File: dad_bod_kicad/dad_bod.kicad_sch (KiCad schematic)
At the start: 67 parts

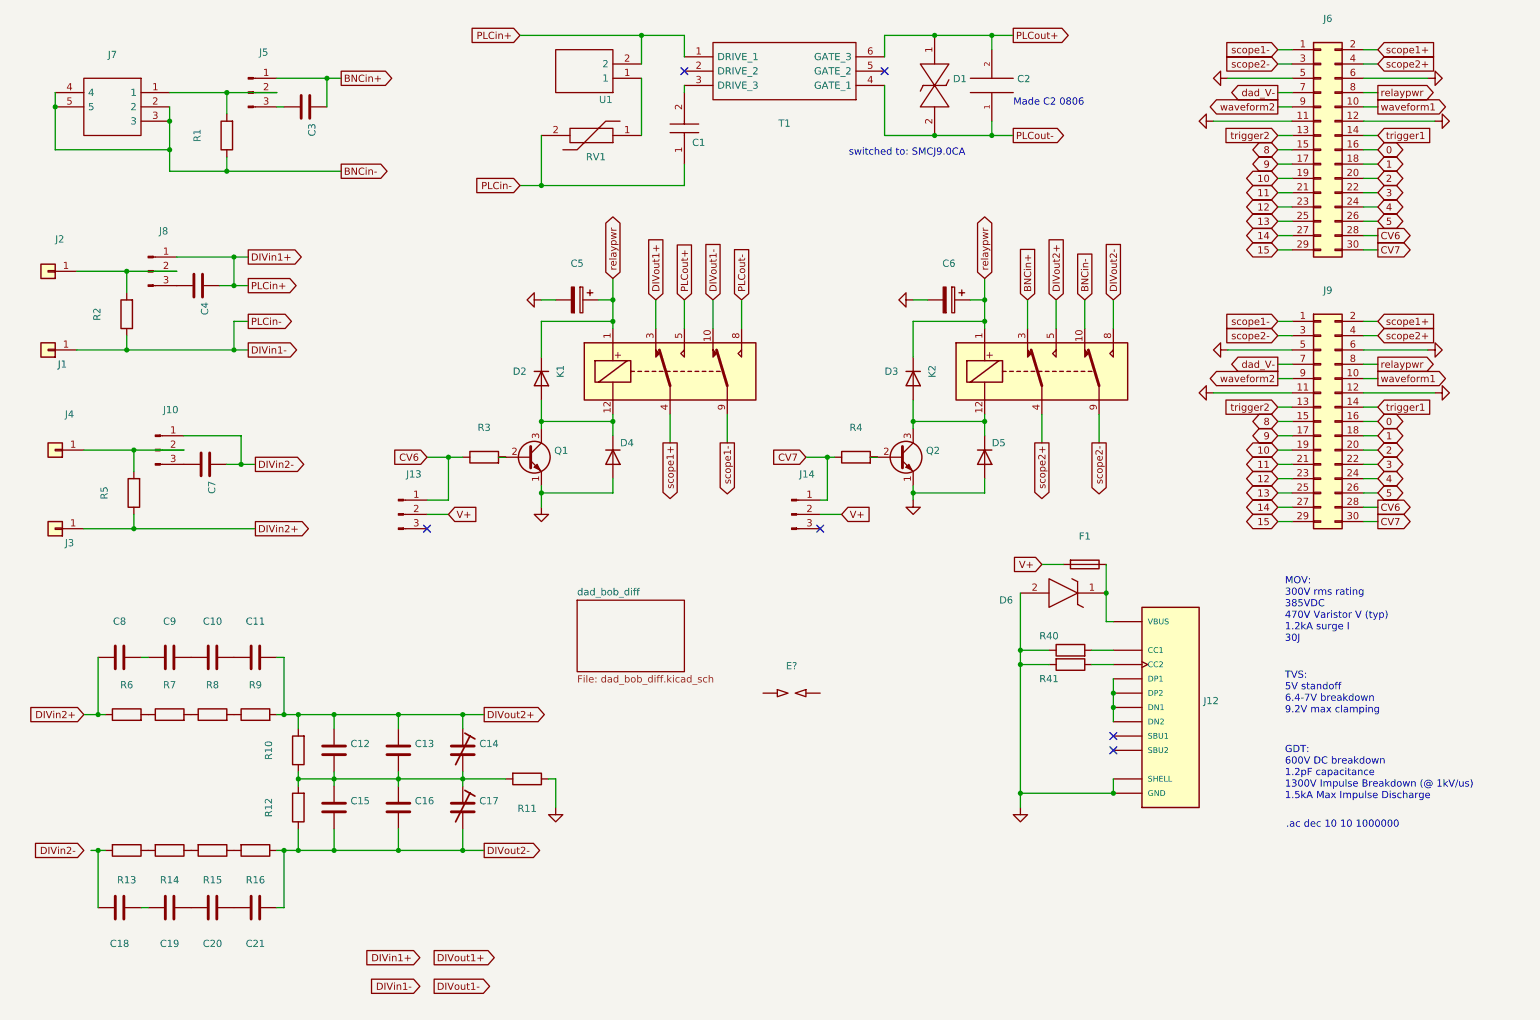
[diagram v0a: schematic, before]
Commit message: Routed PCB, layout needs rework, forked to dad_bod
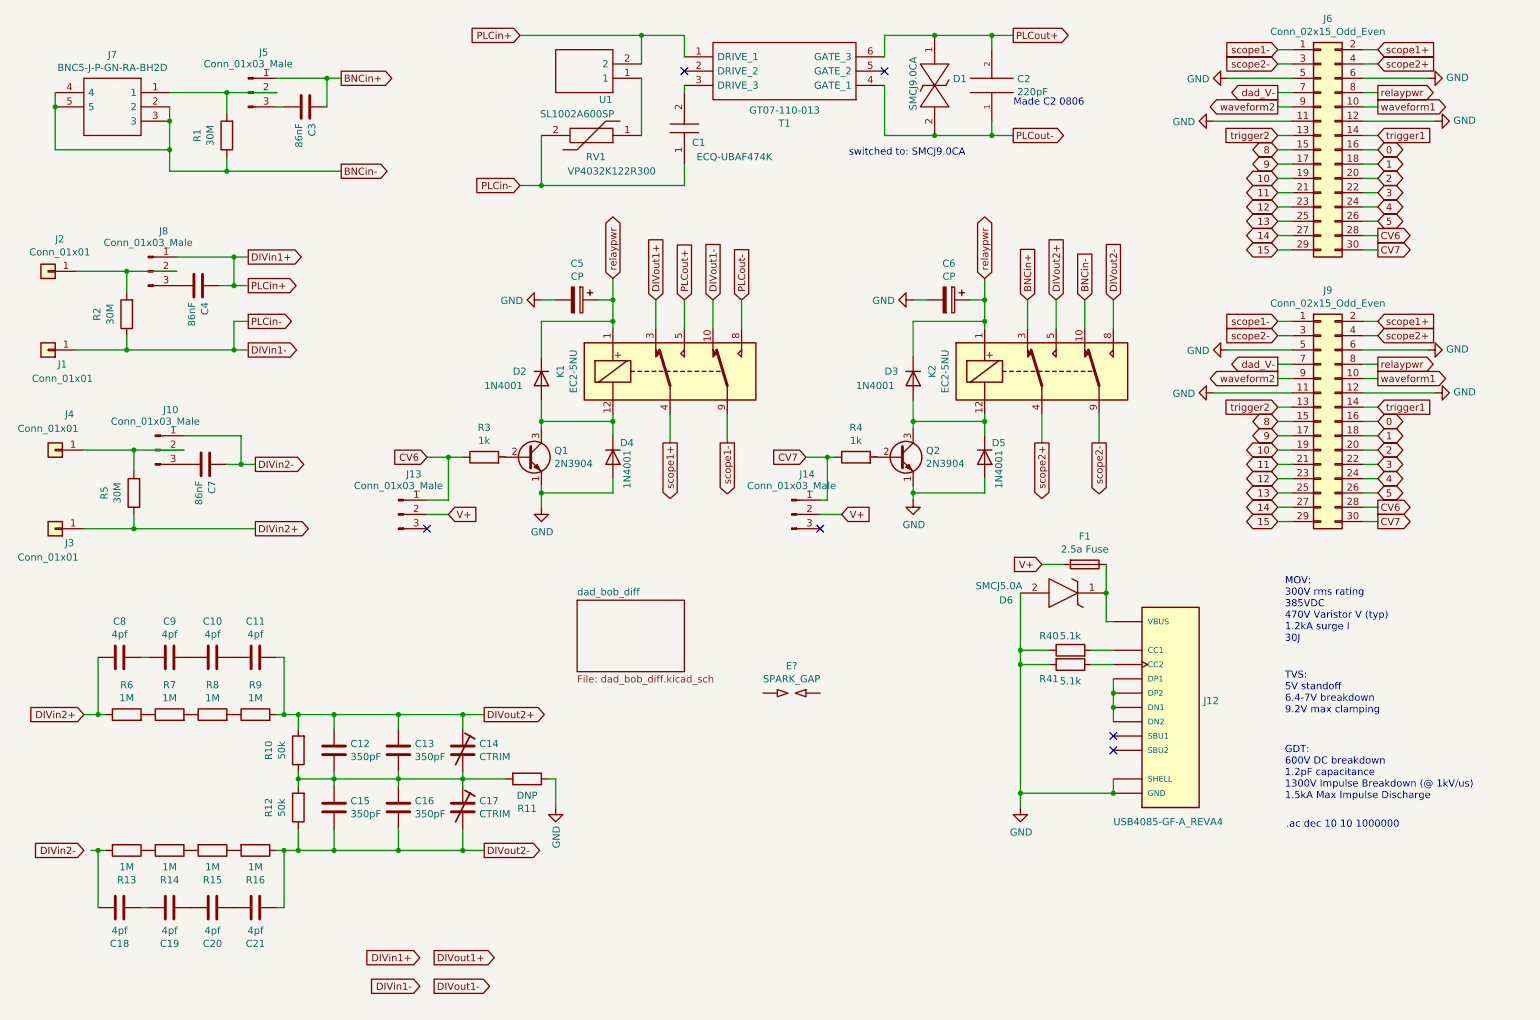
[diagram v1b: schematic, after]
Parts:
- C1: value (none) -> ECQ-UBAF474K; footprint (none) -> ECQUBAF474K
- C10, C11, C18, C19, C20, C21, C8, C9: value (none) -> 4pf; footprint (none) -> Capacitor_SMD:C_0805_2012Metric_Pad1.15x1.40mm_HandSolder
- C12, C13, C15, C16: value (none) -> 350pF; footprint (none) -> Capacitor_SMD:C_0805_2012Metric_Pad1.15x1.40mm_HandSolder
- C14, C17: value (none) -> CTRIM; footprint (none) -> Capacitor_SMD:C_Trimmer_Voltronics_JQ
- C2: value (none) -> 220pF; footprint (none) -> Capacitor_SMD:C_0805_2012Metric_Pad1.15x1.40mm_HandSolder
- C3, C4, C7: value (none) -> 86nF; footprint (none) -> Capacitor_SMD:C_0805_2012Metric_Pad1.15x1.40mm_HandSolder
- C5, C6: value (none) -> CP; footprint (none) -> Capacitor_SMD:C_0805_2012Metric_Pad1.15x1.40mm_HandSolder
- D1: value (none) -> SMCJ9.0CA; footprint (none) -> SMCJ5:DIONM7959X262N
- D2, D3, D4, D5: value (none) -> 1N4001; footprint (none) -> Diode_THT:D_DO-41_SOD81_P10.16mm_Horizontal
- D6: value (none) -> SMCJ5.0A; footprint (none) -> kyuditsky_kicad_fp:littlefuseTVS
- E?: value (none) -> SPARK_GAP
- F1: value (none) -> 2.5a Fuse; footprint (none) -> Resistor_THT:R_Axial_DIN0204_L3.6mm_D1.6mm_P2.54mm_Vertical
- J1, J2, J3, J4: value (none) -> Conn_01x01; footprint (none) -> kyuditsky_kicad_fp:Banana_Jack_S_RA_73099
- J10, J13, J14, J5, J8: value (none) -> Conn_01x03_Male; footprint (none) -> Connector_PinHeader_2.54mm:PinHeader_1x03_P2.54mm_Vertical
- J12: value (none) -> USB4085-GF-A_REVA4; footprint (none) -> GCT_USB4085-GF-A_REVA4
- J6: value (none) -> Conn_02x15_Odd_Even; footprint (none) -> Connector_PinHeader_2.54mm:PinHeader_2x15_P2.54mm_Horizontal
- J7: value (none) -> BNC5-J-P-GN-RA-BH2D; footprint (none) -> BNC5-J-P-GN-RA-BH2D_kicad:BNC5JPGNRABH2D
- J9: value (none) -> Conn_02x15_Odd_Even; footprint (none) -> Connector_PinSocket_2.54mm:PinSocket_2x15_P2.54mm_Horizontal
- K1, K2: value (none) -> EC2-5NU; footprint (none) -> Relay_THT:Relay_DPDT_Kemet_EC2
- Q1, Q2: value (none) -> 2N3904; footprint (none) -> Package_TO_SOT_THT:TO-92_Inline
- R1, R2, R5: value (none) -> 30M; footprint (none) -> Resistor_SMD:R_0805_2012Metric_Pad1.15x1.40mm_HandSolder
- R10, R12: value (none) -> 50k; footprint (none) -> Resistor_SMD:R_0805_2012Metric_Pad1.15x1.40mm_HandSolder
- R11: value (none) -> DNP; footprint (none) -> Resistor_SMD:R_0805_2012Metric_Pad1.15x1.40mm_HandSolder
- R13, R14, R15, R16, R6, R7, R8, R9: value (none) -> 1M; footprint (none) -> Resistor_SMD:R_0805_2012Metric_Pad1.15x1.40mm_HandSolder
- R3, R4: value (none) -> 1k; footprint (none) -> Resistor_SMD:R_0805_2012Metric_Pad1.15x1.40mm_HandSolder
- R40, R41: value (none) -> 5.1k; footprint (none) -> Resistor_SMD:R_0805_2012Metric_Pad1.15x1.40mm_HandSolder
- RV1: value (none) -> VP4032K122R300; footprint (none) -> VP4032K122R300_kicad:CAPPM10080X500N
- T1: value (none) -> GT07-110-013; footprint (none) -> kyuditsky_kicad_fp:GT07110013
- U1: value (none) -> SL1002A600SP; footprint (none) -> SL1002A600SP

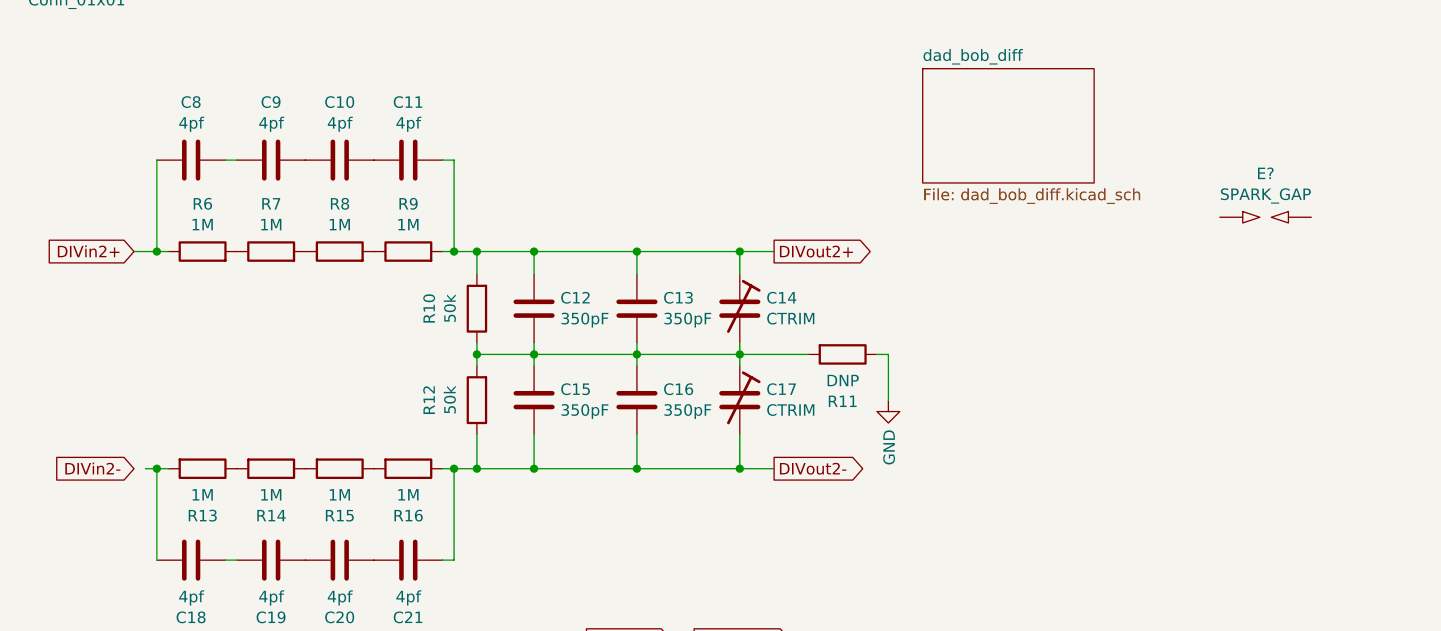
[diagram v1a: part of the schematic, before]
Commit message: fixing scheme & pcb disparities
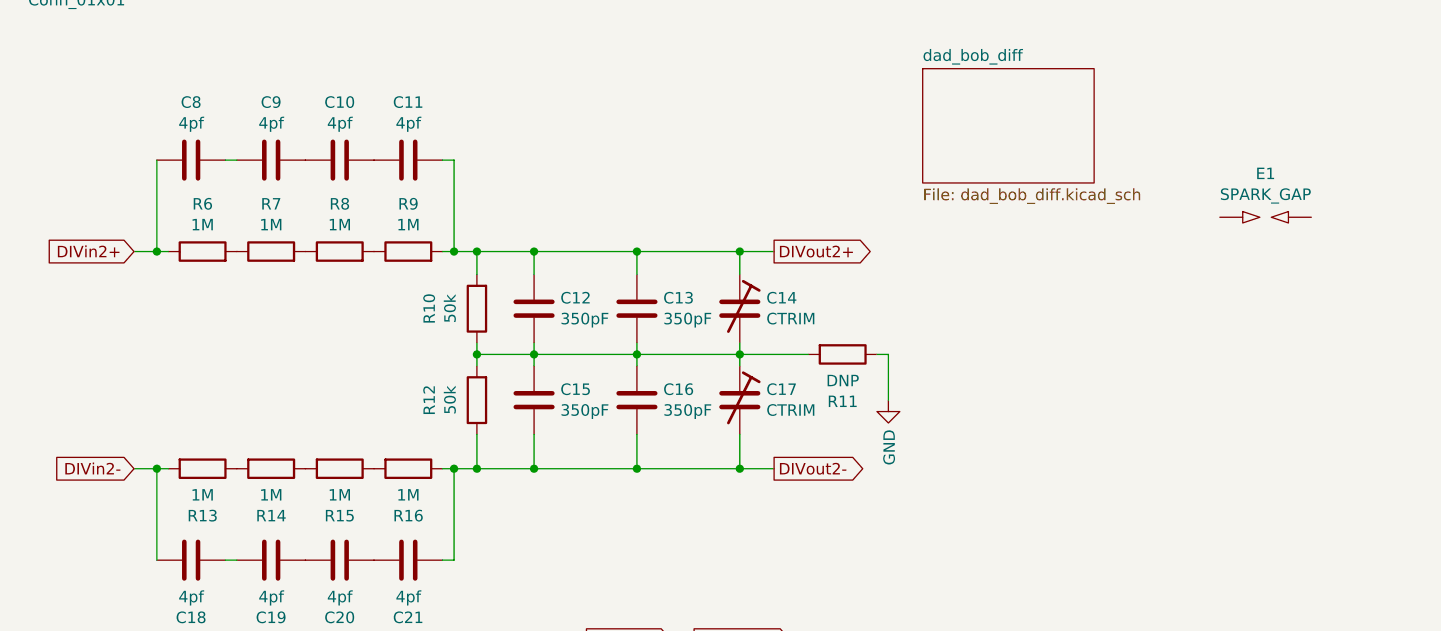
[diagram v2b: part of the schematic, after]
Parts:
- C1: footprint ECQUBAF474K -> kyuditsky_kicad:ECQ-UBAF474K-3_side
- D2, D3, D4, D5: footprint Diode_THT:D_DO-41_SOD81_P10.16mm_Horizontal -> Diode_THT:D_DO-41_SOD81_P2.54mm_Vertical_KathodeUp
- gave numbers to parts that had none: 1
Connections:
- net DIVin2-: now also C18.1, R13.2
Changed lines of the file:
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@@
     (stroke (width 0) (type default) (color 0 0 0 0))
   )
-  (wire (pts (xy 30.48 166.37) (xy 29.21 166.37))
+  (wire (pts (xy 27.94 166.37) (xy 30.48 166.37))
     (stroke (width 0) (type default) (color 0 0 0 0))
   )
@@
     (property "Reference" "C1" (id 0) (at 137.16 40.64 90))
     (property "Value" "ECQ-UBAF474K" (id 1) (at 143.51 43.18 90))
-    (property "Footprint" "ECQUBAF474K" (id 2) (at 133.35 35.56 0)
+    (property "Footprint" "kyuditsky_kicad:ECQ-UBAF474K-3_side" (id 2) (at 133.35 35.56 0)
       (effects (font (size 1.27 1.27)) (justify left) hide)
     )
@@
       (effects (font (size 1.27 1.27)) (justify left))
     )
-    (property "Footprint" "Diode_THT:D_DO-41_SOD81_P10.16mm_Horizontal" (id 2) (at 104.775 82.55 0)
+    (property "Footprint" "Diode_THT:D_DO-41_SOD81_P2.54mm_Vertical_KathodeUp" (id 2) (at 104.775 82.55 0)
       (effects (font (size 1.27 1.27)) hide)
     )
@@
       (effects (font (size 1.27 1.27)) (justify left))
     )
-    (property "Footprint" "Diode_THT:D_DO-41_SOD81_P10.16mm_Horizontal" (id 2) (at 117.475 96.52 0)
+    (property "Footprint" "Diode_THT:D_DO-41_SOD81_P2.54mm_Vertical_KathodeUp" (id 2) (at 117.475 96.52 0)
       (effects (font (size 1.27 1.27)) hide)
     )
@@
       (effects (font (size 1.27 1.27)) (justify left))
     )
-    (property "Footprint" "Diode_THT:D_DO-41_SOD81_P10.16mm_Horizontal" (id 2) (at 170.815 82.55 0)
+    (property "Footprint" "Diode_THT:D_DO-41_SOD81_P2.54mm_Vertical_KathodeUp" (id 2) (at 170.815 82.55 0)
       (effects (font (size 1.27 1.27)) hide)
     )
@@
       (effects (font (size 1.27 1.27)) (justify left))
     )
-    (property "Footprint" "Diode_THT:D_DO-41_SOD81_P10.16mm_Horizontal" (id 2) (at 183.515 96.52 0)
+    (property "Footprint" "Diode_THT:D_DO-41_SOD81_P2.54mm_Vertical_KathodeUp" (id 2) (at 183.515 96.52 0)
       (effects (font (size 1.27 1.27)) hide)
     )
@@
   (symbol (lib_id "dad_bob-rescue:SPARK_GAP-Device") (at 153.67 138.43 0) (unit 1)
     (in_bom yes) (on_board yes)
-    (property "Reference" "E?" (id 0) (at 153.67 133.604 0))
+    (property "Reference" "E1" (id 0) (at 153.67 133.604 0))
     (property "Value" "SPARK_GAP" (id 1) (at 153.67 135.9154 0))
     (property "Footprint" "" (id 2) (at 153.67 140.208 0)
@@
     )
     (path "/00000000-0000-0000-0000-000061cad9e9"
-      (reference "C1") (unit 1) (value "ECQ-UBAF474K") (footprint "ECQUBAF474K")
+      (reference "C1") (unit 1) (value "ECQ-UBAF474K") (footprint "kyuditsky_kicad:ECQ-UBAF474K-3_side")
     )
     (path "/00000000-0000-0000-0000-0000619514be"
@@
     )
     (path "/00000000-0000-0000-0000-0000620ff5ac"
-      (reference "D2") (unit 1) (value "1N4001") (footprint "Diode_THT:D_DO-41_SOD81_P10.16mm_Horizontal")
+      (reference "D2") (unit 1) (value "1N4001") (footprint "Diode_THT:D_DO-41_SOD81_P2.54mm_Vertical_KathodeUp")
     )
     (path "/00000000-0000-0000-0000-0000622492e1"
-      (reference "D3") (unit 1) (value "1N4001") (footprint "Diode_THT:D_DO-41_SOD81_P10.16mm_Horizontal")
+      (reference "D3") (unit 1) (value "1N4001") (footprint "Diode_THT:D_DO-41_SOD81_P2.54mm_Vertical_KathodeUp")
     )
     (path "/00000000-0000-0000-0000-000062103b30"
-      (reference "D4") (unit 1) (value "1N4001") (footprint "Diode_THT:D_DO-41_SOD81_P10.16mm_Horizontal")
+      (reference "D4") (unit 1) (value "1N4001") (footprint "Diode_THT:D_DO-41_SOD81_P2.54mm_Vertical_KathodeUp")
     )
     (path "/00000000-0000-0000-0000-0000622492e7"
-      (reference "D5") (unit 1) (value "1N4001") (footprint "Diode_THT:D_DO-41_SOD81_P10.16mm_Horizontal")
+      (reference "D5") (unit 1) (value "1N4001") (footprint "Diode_THT:D_DO-41_SOD81_P2.54mm_Vertical_KathodeUp")
     )
     (path "/00000000-0000-0000-0000-0000625e9666"
@@
     )
     (path "/00000000-0000-0000-0000-000062690ea2"
-      (reference "E?") (unit 1) (value "SPARK_GAP") (footprint "")
+      (reference "E1") (unit 1) (value "SPARK_GAP") (footprint "")
     )
     (path "/00000000-0000-0000-0000-0000626099aa"
@@
     )
     (path "/00000000-0000-0000-0000-0000624874cf/00000000-0000-0000-0000-000062401c8f"
-      (reference "FB1") (unit 1) (value "Ferrite_Bead") (footprint "Ferrite_THT:LairdTech_28C0236-0JW-10")
+      (reference "FB1") (unit 1) (value "Ferrite_Bead") (footprint "Resistor_SMD:R_0805_2012Metric_Pad1.20x1.40mm_HandSolder")
     )
     (path "/00000000-0000-0000-0000-0000624874cf/00000000-0000-0000-0000-00006240916c"
-      (reference "FB2") (unit 1) (value "Ferrite_Bead") (footprint "Ferrite_THT:LairdTech_28C0236-0JW-10")
+      (reference "FB2") (unit 1) (value "Ferrite_Bead") (footprint "Resistor_SMD:R_0805_2012Metric_Pad1.20x1.40mm_HandSolder")
     )
     (path "/00000000-0000-0000-0000-0000624874cf/00000000-0000-0000-0000-00006240281d"
-      (reference "FB3") (unit 1) (value "Ferrite_Bead") (footprint "Ferrite_THT:LairdTech_28C0236-0JW-10")
+      (reference "FB3") (unit 1) (value "Ferrite_Bead") (footprint "Resistor_SMD:R_0805_2012Metric_Pad1.20x1.40mm_HandSolder")
     )
     (path "/00000000-0000-0000-0000-000062138511"

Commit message: Routed board
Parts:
- J9: footprint Connector_PinSocket_2.54mm:PinSocket_2x15_P2.54mm_Horizontal -> Connector_PinSocket_2.54mm:PinSocket_2x15_P2.54mm_Vertical
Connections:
- net 0: now also J9.15 (Pin_15); no longer J9.16 (Pin_16)
- net 1: now also J9.17 (Pin_17); no longer J9.18 (Pin_18)
- net 10: now also J9.20 (Pin_20); no longer J9.19 (Pin_19)
- net 11: now also J9.22 (Pin_22); no longer J9.21 (Pin_21)
- net 12: now also J9.24 (Pin_24); no longer J9.23 (Pin_23)
- net 13: now also J9.26 (Pin_26); no longer J9.25 (Pin_25)
- net 14: now also J9.28 (Pin_28); no longer J9.27 (Pin_27)
- net 15: now also J9.30 (Pin_30); no longer J9.29 (Pin_29)
- net 2: now also J9.19 (Pin_19); no longer J9.20 (Pin_20)
- net 3: now also J9.21 (Pin_21); no longer J9.22 (Pin_22)
- net 4: now also J9.23 (Pin_23); no longer J9.24 (Pin_24)
- net 5: now also J9.25 (Pin_25); no longer J9.26 (Pin_26)
- net 8: now also J9.16 (Pin_16); no longer J9.15 (Pin_15)
- net 9: now also J9.18 (Pin_18); no longer J9.17 (Pin_17)
- net CV6: now also J9.27 (Pin_27); no longer J9.28 (Pin_28), R3.1
- net CV7: now also J9.29 (Pin_29); no longer J9.30 (Pin_30), R4.1
- net GND: no longer R11.1
- net V+: now also J13.3 (Pin_3), J14.3 (Pin_3); no longer J13.2 (Pin_2), J14.2 (Pin_2)
- net dad_V-: now also J9.8 (Pin_8); no longer J9.7 (Pin_7)
- net relaypwr: now also J9.7 (Pin_7); no longer J9.8 (Pin_8)
- net scope1+: now also J9.1 (Pin_1); no longer J9.2 (Pin_2)
- net scope1-: now also J9.2 (Pin_2); no longer J9.1 (Pin_1)
- net scope2+: now also J9.3 (Pin_3); no longer J9.4 (Pin_4)
- net scope2-: now also J9.4 (Pin_4); no longer J9.3 (Pin_3)
- net trigger1: now also J9.13 (Pin_13); no longer J9.14 (Pin_14)
- net trigger2: now also J9.14 (Pin_14); no longer J9.13 (Pin_13)
- net waveform1: now also J9.9 (Pin_9); no longer J9.10 (Pin_10)
- net waveform2: now also J9.10 (Pin_10); no longer J9.9 (Pin_9)
- new net: J13.2 (Pin_2), R3.1
- new net: J14.2 (Pin_2), R4.1
- new net GNDREF: R11.1
- no-connect marks 6 -> 4
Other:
- moved on the sheet: J13, J14
